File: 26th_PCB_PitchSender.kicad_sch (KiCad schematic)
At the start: 15 parts, among them J1 Amp, J2 Conn_01x04_Pin, J3 microSD, J4 Conn_01x04_Socket, J5 BNO055, J6 BMP390

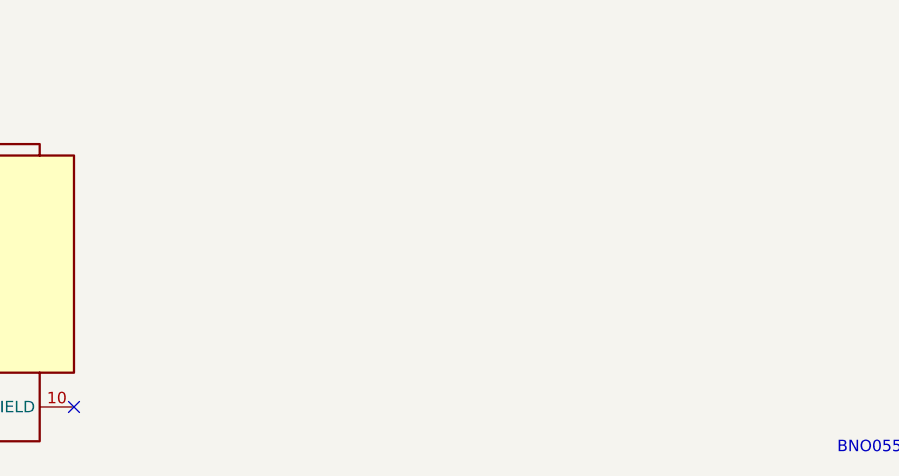
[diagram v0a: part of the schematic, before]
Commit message: Add IMU
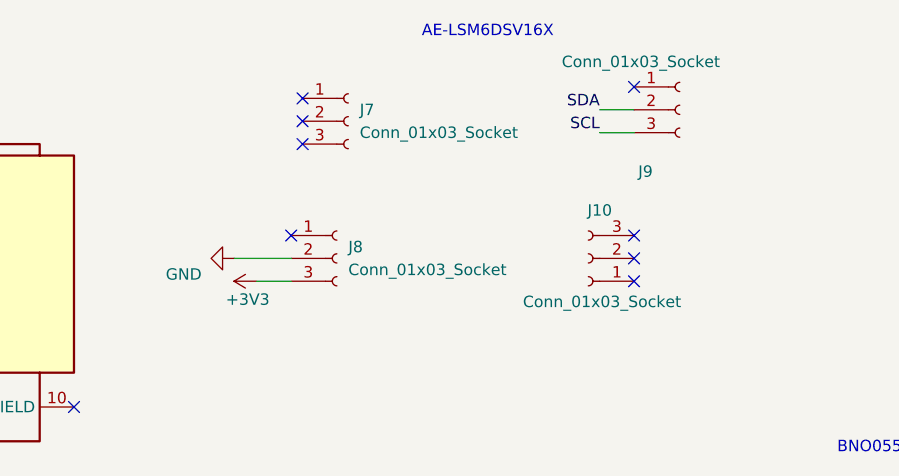
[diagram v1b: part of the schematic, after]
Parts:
- added J10, J7, J8, J9: Conn_01x03_Socket, Connector_PinSocket_2.54mm:PinSocket_1x03_P2.54mm_Vertical, symbol Connector:Conn_01x03_Socket
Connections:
- net +3V3: now also J8.3 (Pin_3)
- net GND: now also J8.2 (Pin_2)
- net SCL: now also J9.3 (Pin_3)
- net SDA: now also J9.2 (Pin_2)
- no-connect marks 30 -> 38
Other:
- note added: "AE-LSM6DSV16X"
